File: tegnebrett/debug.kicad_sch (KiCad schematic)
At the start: 28 parts, among them J6 FPGA_Header_Pin, U1 XC7A100T-2FTG256I, U2 Oscillator 100MHz, U8 IS66WVH16M8DBLL-100B1LI1

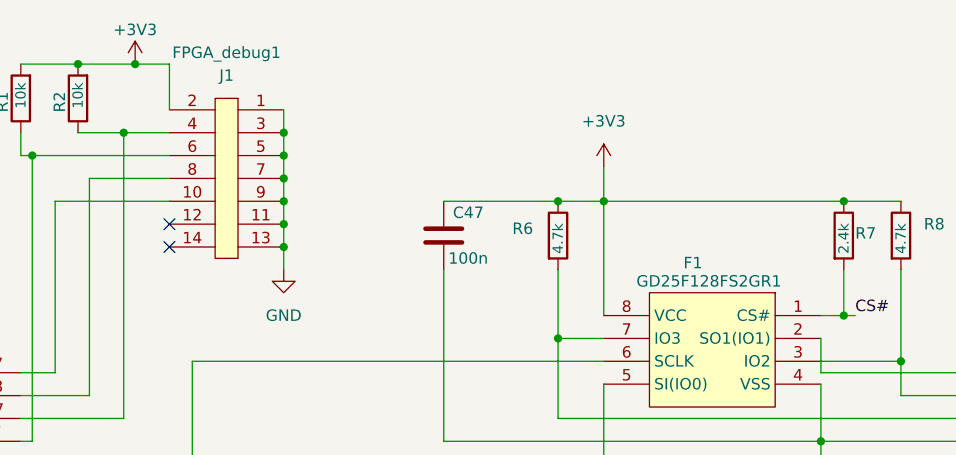
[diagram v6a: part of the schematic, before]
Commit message: feat: add FPGA flash footprint, import to PCB
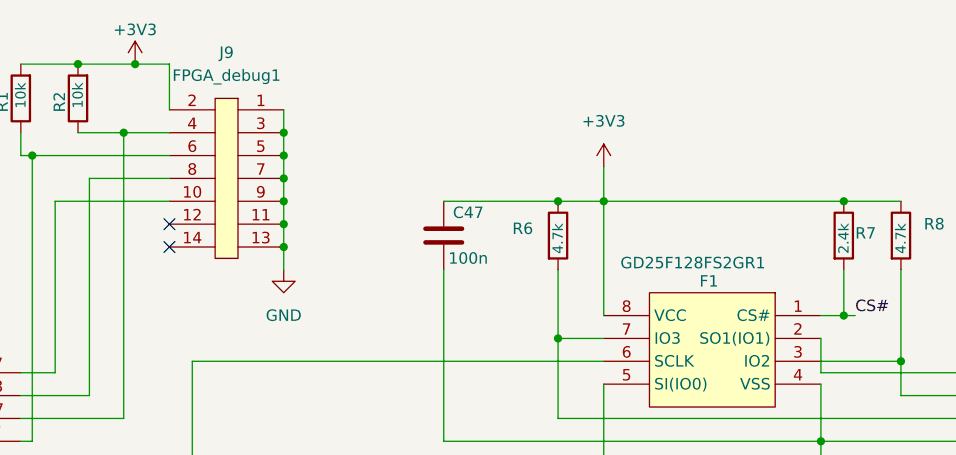
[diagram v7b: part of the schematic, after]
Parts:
- F1: renamed from GD25F128FS2GR1; value F1 -> GD25F128FS2GR1; footprint (none) -> tegnebrett_modules:flash_tegnebrett
- J9: renamed from FPGA_debug1; value J1 -> FPGA_debug1
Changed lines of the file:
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@@
 		(on_board yes)
 		(dnp no)
-		(property "Reference" "FPGA_debug1"
+		(property "Reference" "J9"
 			(at 107.95 17.78 0)
 			(effects
@@
 			)
 		)
-		(property "Value" "J1"
+		(property "Value" "FPGA_debug1"
 			(at 107.95 20.32 0)
 			(effects
@@
 			(project "getting-started"
 				(path "/d9a31669-c5f1-42a7-9461-3df04b9a4e62/5e0df967-c6b5-4cdf-8fe6-93251df44e99"
-					(reference "FPGA_debug1")
+					(reference "J9")
 					(unit 1)
 				)
@@
 		(on_board yes)
 		(dnp no)
-		(property "Reference" "GD25F128FS2GR1"
+		(property "Reference" "F1"
 			(at 161.544 43.18 0)
 			(effects
@@
 			)
 		)
-		(property "Value" "F1"
+		(property "Value" "GD25F128FS2GR1"
 			(at 159.766 41.148 0)
 			(effects
@@
 			)
 		)
-		(property "Footprint" ""
+		(property "Footprint" "tegnebrett_modules:flash_tegnebrett"
 			(at 161.29 44.45 0)
 			(effects
@@
 			(project "getting-started"
 				(path "/d9a31669-c5f1-42a7-9461-3df04b9a4e62/5e0df967-c6b5-4cdf-8fe6-93251df44e99"
-					(reference "GD25F128FS2GR1")
+					(reference "F1")
 					(unit 1)
 				)

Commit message: feat: add 48MHz crystal footprint + add to PCB
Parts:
- D2, D3, D4: footprint (none) -> tegnebrett_modules:LED_J-SERIES_3030_CRW-M
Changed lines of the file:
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@@
 			)
 		)
-		(property "Footprint" ""
+		(property "Footprint" "tegnebrett_modules:LED_J-SERIES_3030_CRW-M"
 			(at 365.76 170.18 0)
 			(effects
@@
 			)
 		)
-		(property "Footprint" ""
+		(property "Footprint" "tegnebrett_modules:LED_J-SERIES_3030_CRW-M"
 			(at 339.09 167.64 0)
 			(effects
@@
 			)
 		)
-		(property "Footprint" ""
+		(property "Footprint" "tegnebrett_modules:LED_J-SERIES_3030_CRW-M"
 			(at 339.09 172.72 0)
 			(effects
